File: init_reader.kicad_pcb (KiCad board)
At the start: 2 copper layers, 95 x 60 mm, 0 parts

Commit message: update schematics
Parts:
- added A1: RaspberryPi_Pico_W, Module:RaspberryPi_Pico_W_SMD_HandSolder, F.Cu at (123.9, 74.0)
- added BT1: Battery, Battery:BatteryHolder_MPD_BA9VPC_1xPP3, F.Cu at (128.2, 123.7)
- added C1: 10uF, Capacitor_THT:CP_Radial_D5.0mm_P2.50mm, F.Cu at (183.0, 87.0)
- added C2: 10uF, Capacitor_THT:CP_Radial_D5.0mm_P2.50mm, F.Cu at (176.0, 87.0)
- added C3: 10uF, Capacitor_THT:CP_Radial_D5.0mm_P2.50mm, F.Cu at (166.0, 96.5)
- added C4: 10uF, Capacitor_THT:CP_Radial_D5.0mm_P2.50mm, F.Cu at (169.0, 87.0)
- added J1: DE9_Pins, Connector_Dsub:DSUB-9_Pins_Horizontal_P2.77x2.84mm_EdgePinOffset7.70mm_Housed_MountingHolesOffset9.12mm, F.Cu at (187.2, 80.5)
- added R1: R, Resistor_THT:R_Axial_DIN0207_L6.3mm_D2.5mm_P7.62mm_Horizontal, F.Cu at (122.1, 55.5)
- added U1: LCD_16x4, 0_moje:AC-164A, F.Cu at (151.0, 77.5)
- added U2: MAX232, Package_DIP:DIP-16_W7.62mm, F.Cu at (183.2, 103.4)
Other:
- board outline removed

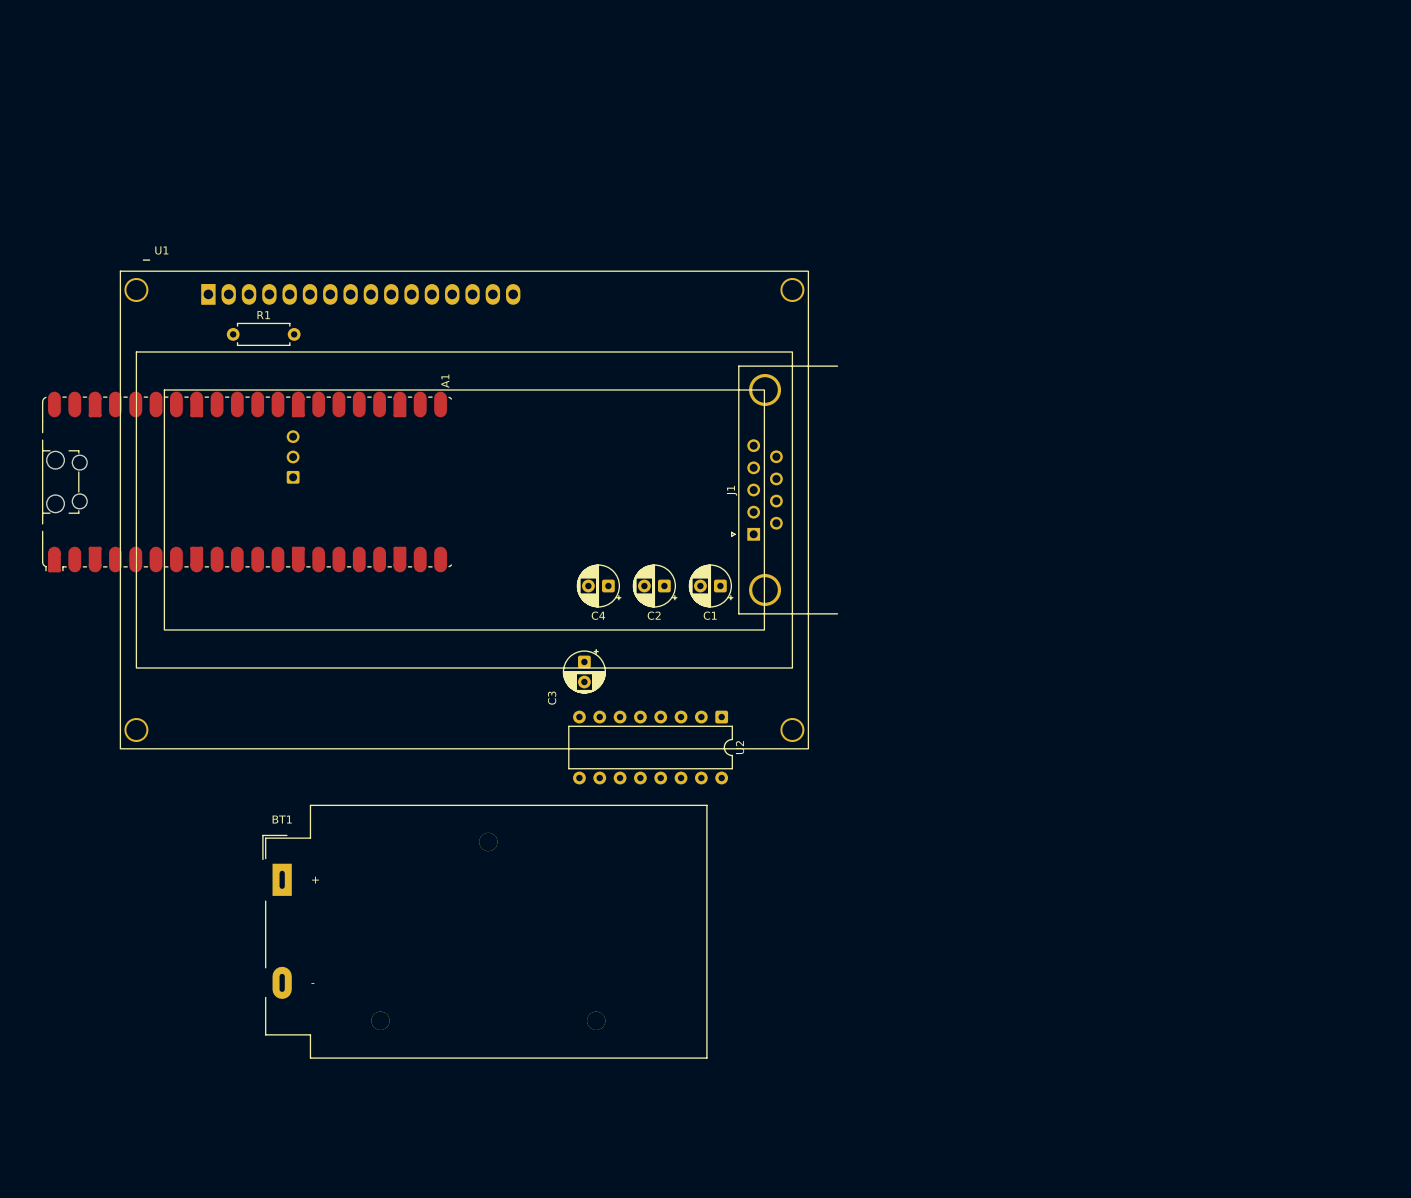
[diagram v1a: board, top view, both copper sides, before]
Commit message: add all components - basic circuit
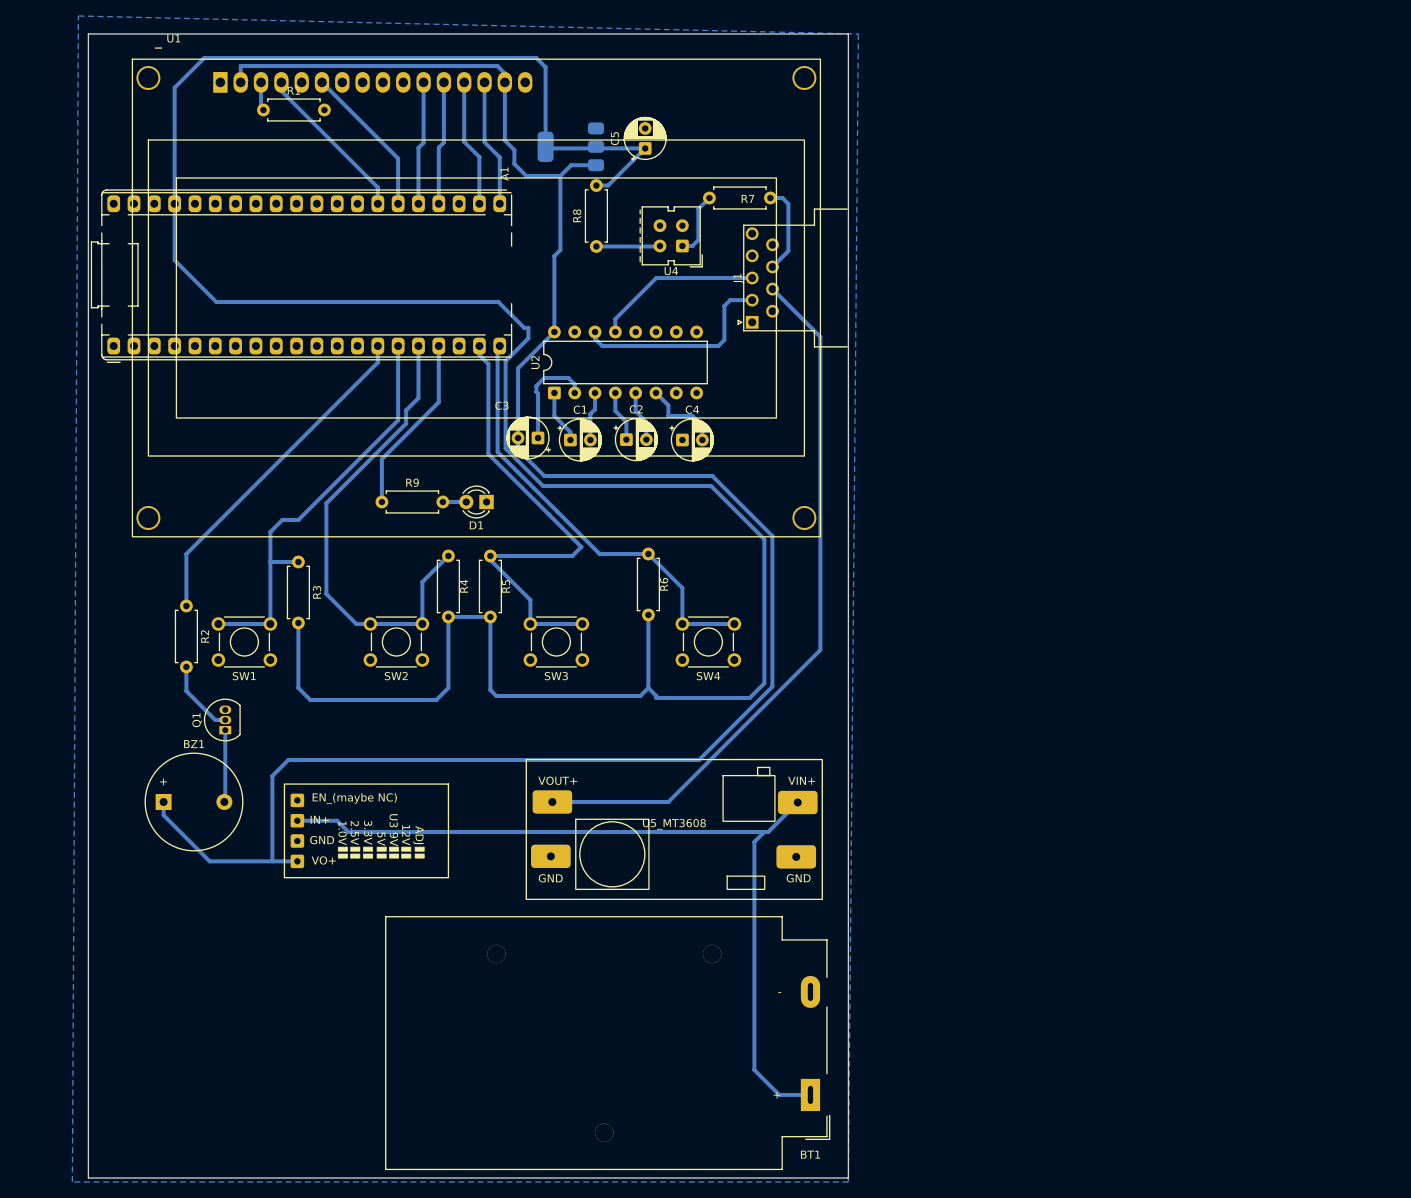
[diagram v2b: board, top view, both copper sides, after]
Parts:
- added BZ1: Buzzer, Buzzer_Beeper:Buzzer_12x9.5RM7.6, F.Cu at (113.4, 114.0)
- added C5: 1uF, Capacitor_THT:CP_Radial_D5.0mm_P2.50mm, F.Cu at (173.6, 32.3)
- added D1: LED, LED_THT:LED_D3.0mm, F.Cu at (153.8, 76.5)
- added Q1: Q_NPN, Package_TO_SOT_THT:TO-92_Inline, F.Cu at (121.1, 105.0)
- added R2: 470R, Resistor_THT:R_Axial_DIN0207_L6.3mm_D2.5mm_P7.62mm_Horizontal, F.Cu at (116.2, 89.5)
- added R3: 10k, Resistor_THT:R_Axial_DIN0207_L6.3mm_D2.5mm_P7.62mm_Horizontal, F.Cu at (130.2, 84.0)
- added R4: 10k, Resistor_THT:R_Axial_DIN0207_L6.3mm_D2.5mm_P7.62mm_Horizontal, F.Cu at (149.0, 83.2)
- added R5: 10k, Resistor_THT:R_Axial_DIN0207_L6.3mm_D2.5mm_P7.62mm_Horizontal, F.Cu at (154.2, 83.2)
- added R6: 10k, Resistor_THT:R_Axial_DIN0207_L6.3mm_D2.5mm_P7.62mm_Horizontal, F.Cu at (174.0, 83.0)
- added R7: 2k9, Resistor_THT:R_Axial_DIN0207_L6.3mm_D2.5mm_P7.62mm_Horizontal, F.Cu at (189.2, 38.5)
- added R8: 470R, Resistor_THT:R_Axial_DIN0207_L6.3mm_D2.5mm_P7.62mm_Horizontal, F.Cu at (167.5, 44.6)
- added R9: 240R, Resistor_THT:R_Axial_DIN0207_L6.3mm_D2.5mm_P7.62mm_Horizontal, F.Cu at (140.7, 76.5)
- added SW1: 1, Button_Switch_THT:SW_TH_Tactile_Omron_B3F-100x, F.Cu at (126.8, 96.2)
- added SW2: 2, Button_Switch_THT:SW_TH_Tactile_Omron_B3F-100x, F.Cu at (145.8, 96.2)
- added SW3: 3, Button_Switch_THT:SW_TH_Tactile_Omron_B3F-100x, F.Cu at (165.8, 96.2)
- added SW4: 4, Button_Switch_THT:SW_TH_Tactile_Omron_B3F-100x, F.Cu at (184.8, 96.2)
- added U3: 5V, 00_dc_dc:dc-dc-HW613, F.Cu at (138.7, 117.6)
- added U4: Optocoupler_DC_PhotoNPN_AKEC, OptoDevice:Vishay_CNY70, F.Cu at (178.2, 44.5)
- added U5_MT3608: +24V, 00_dc_dc:dc_dc_MT3608, F.Cu at (177.2, 117.2)
- added U6: AMS1117-3.3, Package_TO_SOT_SMD:SOT-223-3_TabPin2, B.Cu at (164.3, 32.1)
- A1: footprint Module:RaspberryPi_Pico_W_SMD_HandSolder -> 00_ruzne:RaspberryPi_Pico_Common_THT
- BT1: value Battery -> Battery 9V
- J1: footprint Connector_Dsub:DSUB-9_Pins_Horizontal_P2.77x2.84mm_EdgePinOffset7.70mm_Housed_MountingHolesOffset9.12mm -> Connector_Dsub:DSUB-9_Pins_Horizontal_P2.77x2.54mm_EdgePinOffset9.40mm
- moved BT1 71.3 mm to (194.3, 150.6), turned to 180 degrees
- moved U2 45.6 mm to (162.2, 62.9), turned to 90 degrees
- moved C3 28.6 mm to (160.2, 68.5), turned to 180 degrees
- moved R1 28.3 mm to (125.9, 27.5)
- moved U1 26.5 mm to (152.5, 51.0)
- moved J1 26.5 mm to (187.0, 54.0)
- moved C1 26.2 mm to (164.2, 68.8), turned to 0 degrees
- moved A1 23.9 mm to (107.2, 57.0)
- moved C4 20.5 mm to (178.2, 68.8), turned to 0 degrees
- moved C2 18.9 mm to (171.2, 68.7), turned to 0 degrees
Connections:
- A1 pad 14: unconnected-(A1-GPIO10-Pad14) -> BZZ
- A1 pad 15: unconnected-(A1-GPIO11-Pad15) -> GP11
- A1 pad 16: unconnected-(A1-GPIO12-Pad16) -> GP12
- A1 pad 17: unconnected-(A1-GPIO13-Pad17) -> GP13
- A1 pad 19: unconnected-(A1-GPIO14-Pad19) -> GP14
- A1 pad 20: unconnected-(A1-GPIO15-Pad20) -> GP15
- A1 pad 37: unconnected-(A1-3V3_EN-Pad37) -> +3.3V
- BT1 pad 1: unconnected-(BT1-+-Pad1) -> +9V
- BT1 pad 2: unconnected-(BT1---Pad2) -> GND
- J1 pad 6: unconnected-(J1-Pad6) -> GND
- J1 pad 7: unconnected-(J1-Pad7) -> +24V
- J1 pad 8: unconnected-(J1-Pad8) -> Present
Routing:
- net +3.3V: track 0.00 -> 316.4 mm
- net +5V: track 0.00 -> 248.8 mm
- net +9V: track 0.00 -> 103.2 mm
- net +24V: track 0.00 -> 89.0 mm
- net GP14: track 0.00 -> 59.3 mm
- net GP12: track 0.00 -> 59.2 mm
- net GP15: track 0.00 -> 54.5 mm
- net GP11: track 0.00 -> 52.5 mm
- net BZZ: track 0.00 -> 42.4 mm
- net T1IN: track 0.00 -> 25.7 mm
- net GP13: track 0.00 -> 22.4 mm
- net R1IN: track 0.00 -> 20.8 mm
- net RS: track 0.00 -> 20.2 mm
- net En: track 0.00 -> 19.1 mm
- net DB7: track 0.00 -> 16.0 mm
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- added copper zone on B.Cu, net GND
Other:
- board outline added: 95 x 143 mm

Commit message: update all
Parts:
- U4: footprint OptoDevice:Vishay_CNY70 -> Package_DIP:DIP-4_W7.62mm
- moved R1 129.2 mm to (254.1, 43.4), turned to 90 degrees
- moved A1 121.7 mm to (226.0, 30.8), turned to 0 degrees
- moved U6 103.0 mm to (250.9, 87.9), turned to 90 degrees
- moved C5 100.8 mm to (250.7, 97.2), turned to 0 degrees
- moved BZ1 95.0 mm to (169.0, 37.0), turned to -90 degrees
- moved R2 91.9 mm to (193.5, 39.8), turned to 180 degrees
- moved R8 84.9 mm to (238.5, 91.1), turned to 0 degrees
- moved U1 83.3 mm to (232.0, 76.1), turned to -90 degrees
- moved U4 83.2 mm to (238.5, 101.8), turned to 90 degrees
- moved Q1 82.9 mm to (178.0, 44.7), turned to 0 degrees
- moved R7 80.0 mm to (230.8, 106.8), turned to 0 degrees
- moved SW1 75.6 mm to (186.8, 50.3), turned to 90 degrees
- moved R3 74.4 mm to (199.1, 55.7), turned to 180 degrees
- moved J1 70.4 mm to (229.0, 110.6), turned to 0 degrees
- moved BT1 70.0 mm to (132.4, 117.8), turned to 90 degrees
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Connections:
- A1 pad 1: unconnected-(A1-GPIO0-Pad1) -> T1OUT
- A1 pad 2: unconnected-(A1-GPIO1-Pad2) -> R1OUT
- A1 pad 9: unconnected-(A1-GPIO6-Pad9) -> Present_mcu
- J1 pad 1: unconnected-(J1-Pad1) -> Present
- J1 pad 2: T1IN -> R1IN
- J1 pad 3: R1IN -> T1IN
- J1 pad 8: Present -> unconnected-(J1-Pad8)
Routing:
- net T1OUT: track 0.00 -> 77.0 mm, vias 0 -> 2
- net R1OUT: track 0.00 -> 68.4 mm, vias 0 -> 2
- net Present_mcu: track 7.97 -> 53.8 mm, vias 0 -> 2
- net GND: track 0.00 -> 23.3 mm, vias 0 -> 6
- net +5V: track 248.8 -> 263.0 mm
- net GP14: track 59.3 -> 45.7 mm
- net Present: track 11.2 -> 4.47 mm
- net GP15: track 54.5 -> 61.2 mm
- net Net-(U1-VO): track 3.57 -> 9.68 mm
- net RS: track 20.2 -> 24.1 mm
- net +24V: track 89.0 -> 92.8 mm
- net Net-(R7-Pad2): track 8.13 -> 5.05 mm
- net R1IN: track 20.8 -> 23.4 mm
- net +3.3V: track 316.4 -> 318.7 mm
- net GP11: track 52.5 -> 54.5 mm
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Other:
- board size 95 x 143 mm -> 143 x 95 mm

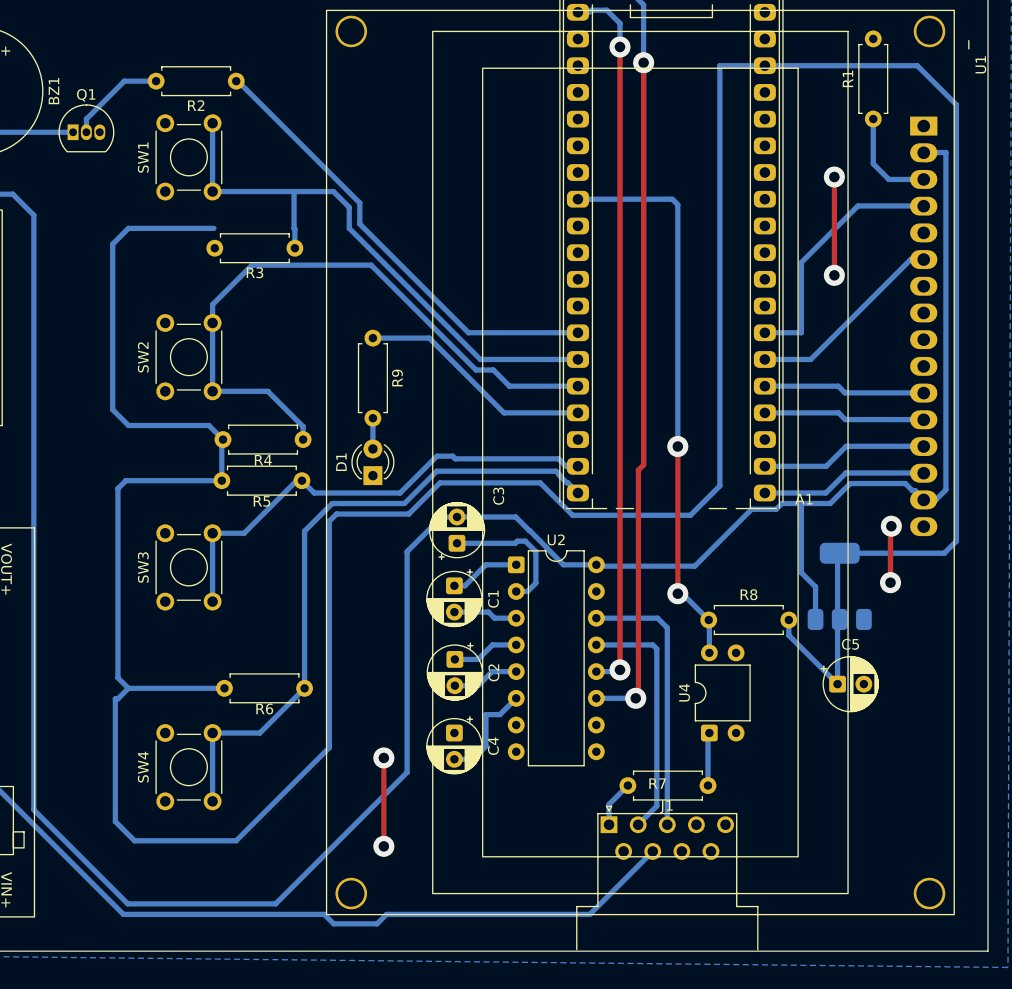
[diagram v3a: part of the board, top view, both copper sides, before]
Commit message: change footprint dsub9 + create cnc folder&files
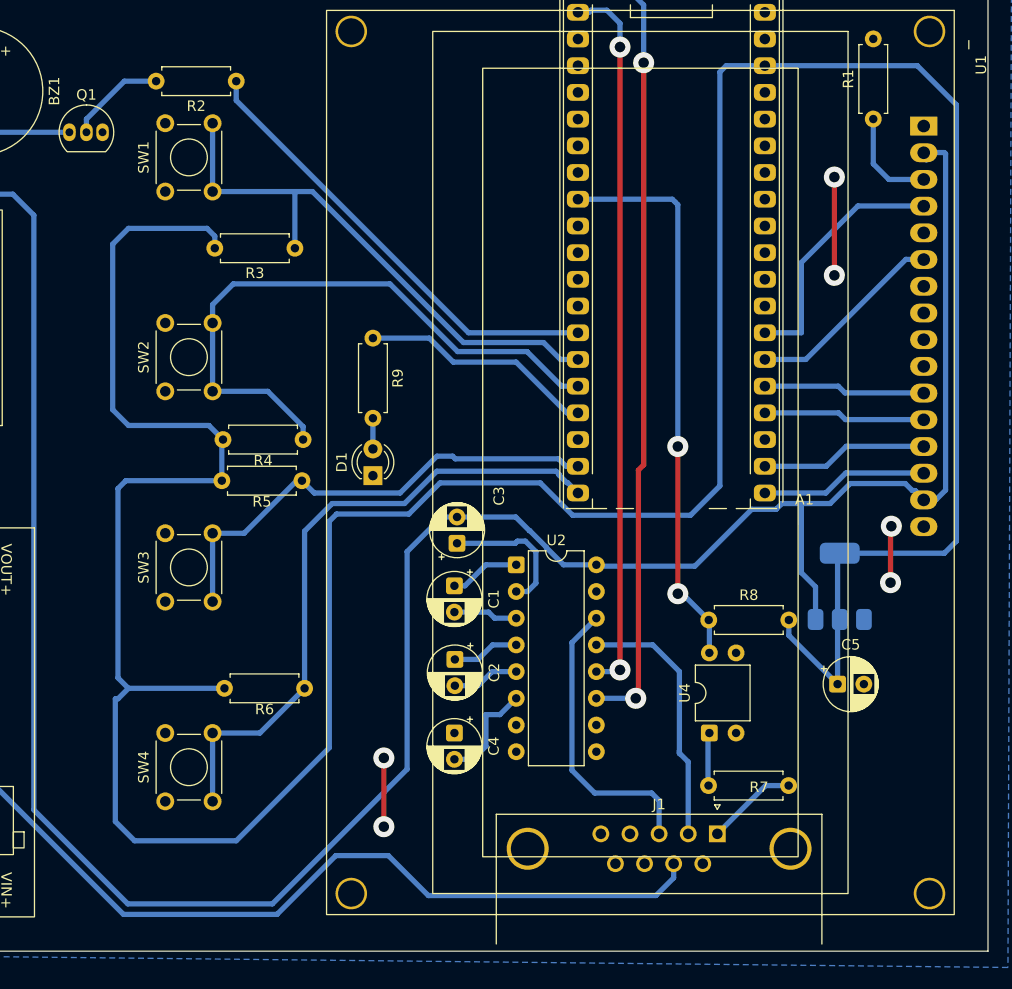
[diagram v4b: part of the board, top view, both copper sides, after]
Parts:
- J1: footprint Connector_Dsub:DSUB-9_Pins_Horizontal_P2.77x2.54mm_EdgePinOffset9.40mm -> Connector_Dsub:DSUB-9_Socket_Horizontal_P2.77x2.84mm_EdgePinOffset7.70mm_Housed_MountingHolesOffset9.12mm
- moved R7 15.3 mm to (246.1, 106.8), turned to 180 degrees
- moved J1 10.3 mm to (239.3, 111.4)
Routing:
- net +24V: track 92.8 -> 97.5 mm
- net Present: track 4.47 -> 8.68 mm
- net T1IN: track 25.9 -> 28.1 mm
- net GND: track 23.3 -> 21.4 mm
- net R1IN: track 23.4 -> 25.0 mm
- net GP12: track 60.6 -> 59.1 mm
- net GP11: track 54.5 -> 53.2 mm
- net +3.3V: track 318.7 -> 319.9 mm
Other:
- rule pad_to_mask_clearance: 0 -> 0.1

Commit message: thick-up all routes and pads
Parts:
- moved R9 1.73 mm to (206.5, 62.5)
- moved C3 0.98 mm to (214.3, 84.7)
- moved D1 0.85 mm to (206.6, 76.5)
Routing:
- net GND: track 21.4 -> 13.5 mm, vias 6 -> 4
- net +5V: track 262.7 -> 256.5 mm
- net RS: track 24.1 -> 21.2 mm
- net GP13: track 22.4 -> 24.2 mm
- net R1OUT: track 68.4 -> 70.1 mm
- net Net-(U2-VS+): track 13.2 -> 14.9 mm
- net T1OUT: track 77.0 -> 78.4 mm
- net DB4: track 15.4 -> 16.5 mm
- net DB6: track 16.0 -> 16.8 mm
- net T1IN: track 28.1 -> 28.8 mm
- net +24V: track 97.5 -> 96.7 mm
- net Net-(U2-VS-): track 10.0 -> 10.7 mm
- net Net-(BZ1--): track 9.03 -> 8.52 mm
